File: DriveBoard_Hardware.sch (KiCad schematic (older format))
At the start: 8 parts

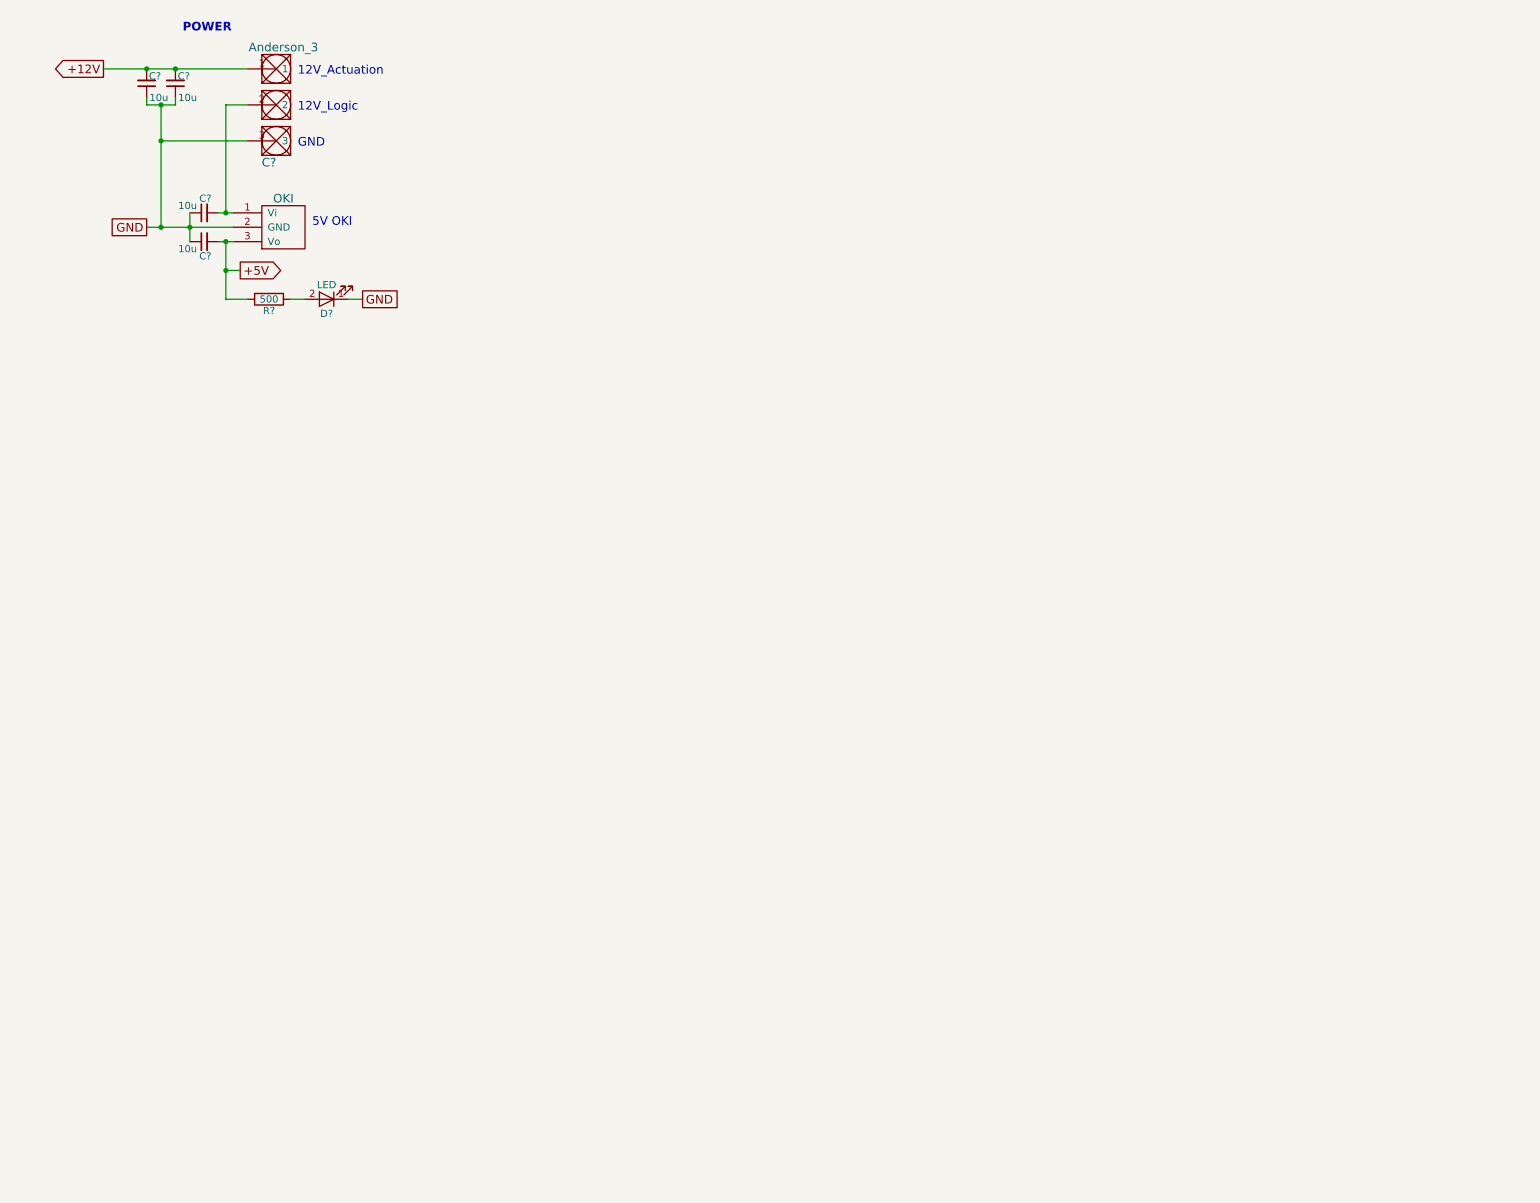
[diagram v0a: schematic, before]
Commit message: Drive Serial Added
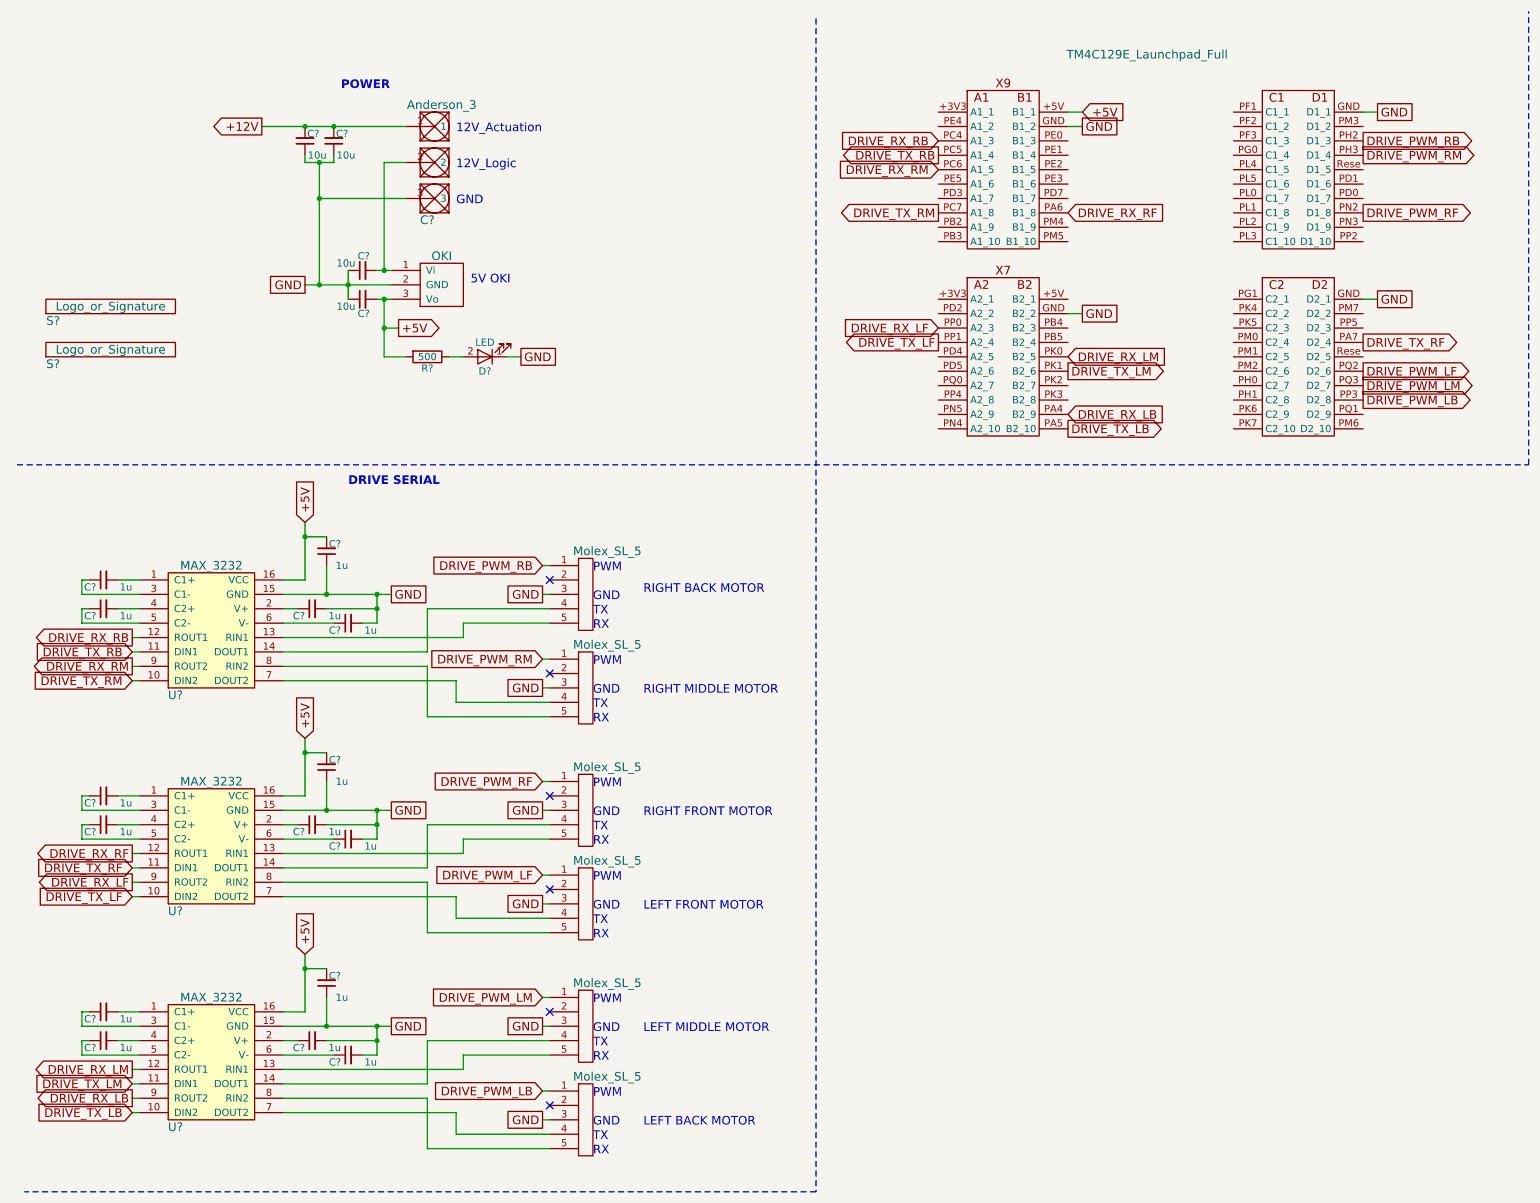
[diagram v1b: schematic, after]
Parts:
- added C? (x15): 1u, symbol C_Small
- added S? (x2): Logo_or_Signature, symbol Logo_or_Signature
- added U? (x3): MAX_3232, symbol MAX_3232
- added U? (x6): Molex_SL_5, symbol Molex_SL_5
- added U?: TM4C129E_Launchpad_Full, symbol TM4C129E_Launchpad_Full
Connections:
- net +5V: now also C?.2, C?.2, C?.2, U?.+5V (B2_1), U?.16 (VCC), U?.16 (VCC), U?.16 (VCC)
- net GND: now also C?.1, C?.1, C?.1, C?.2, C?.2, C?.2, C?.2, C?.2, C?.2, U?.15 (GND), U?.15 (GND), U?.15 (GND), U?.3, U?.3, U?.3, U?.3, U?.3, U?.3, U?.GND (D2_1)
- new net: C?.2, U?.1 (C1+) (x3)
- new net: U?.13 (RIN1), U?.5 (x3)
- new net: U?.14 (DOUT1), U?.4 (x3)
- new net: C?.1, U?.2 (V+) (x3)
- new net: C?.1, U?.3 (C1-) (x3)
- new net: C?.2, U?.4 (C2+) (x3)
- new net: C?.1, U?.5 (C2-) (x3)
- new net: C?.1, U?.6 (V-) (x3)
- new net: U?.4, U?.7 (DOUT2) (x3)
- new net: U?.5, U?.8 (RIN2) (x3)
- new net DRIVE_PWM_LB: U?.1, U?.PP3 (D2_8)
- new net DRIVE_PWM_LF: U?.1, U?.PQ2 (D2_6)
- new net DRIVE_PWM_LM: U?.1, U?.PQ3 (D2_7)
- new net DRIVE_PWM_RB: U?.1, U?.PH2 (D1_3)
- new net DRIVE_PWM_RF: U?.1, U?.PN2 (D1_8)
- new net DRIVE_PWM_RM: U?.1, U?.PH3 (D1_4)
- new net DRIVE_RX_LB: U?.9 (ROUT2), U?.PA4 (B2_9)
- new net DRIVE_RX_LF: U?.9 (ROUT2), U?.PP0 (A2_3)
- new net DRIVE_RX_LM: U?.12 (ROUT1), U?.PK0 (B2_5)
- new net DRIVE_RX_RB: U?.12 (ROUT1), U?.PC4 (A1_3)
- new net DRIVE_RX_RF: U?.12 (ROUT1), U?.PA6 (B1_8)
- new net DRIVE_RX_RM: U?.9 (ROUT2), U?.PC6 (A1_5)
- new net DRIVE_TX_LB: U?.10 (DIN2), U?.PA5 (B2_10)
- new net DRIVE_TX_LF: U?.10 (DIN2), U?.PP1 (A2_4)
- new net DRIVE_TX_LM: U?.11 (DIN1), U?.PK1 (B2_6)
- new net DRIVE_TX_RB: U?.11 (DIN1), U?.PC5 (A1_4)
- new net DRIVE_TX_RF: U?.11 (DIN1), U?.PA7 (D2_4)
- new net DRIVE_TX_RM: U?.10 (DIN2), U?.PC7 (A1_8)
- no-connect marks 0 -> 6
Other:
- note added: "DRIVE SERIAL"
- note added: "LEFT BACK MOTOR"
- note added: "LEFT FRONT MOTOR"
- note added: "LEFT MIDDLE MOTOR"
- note added: "PWM"
- note added: "RIGHT BACK MOTOR"
- note added: "RIGHT FRONT MOTOR"
- note added: "RIGHT MIDDLE MOTOR"
- note added: "RX"
- note added: "TX"
- moved on the sheet: C?, D?, R?

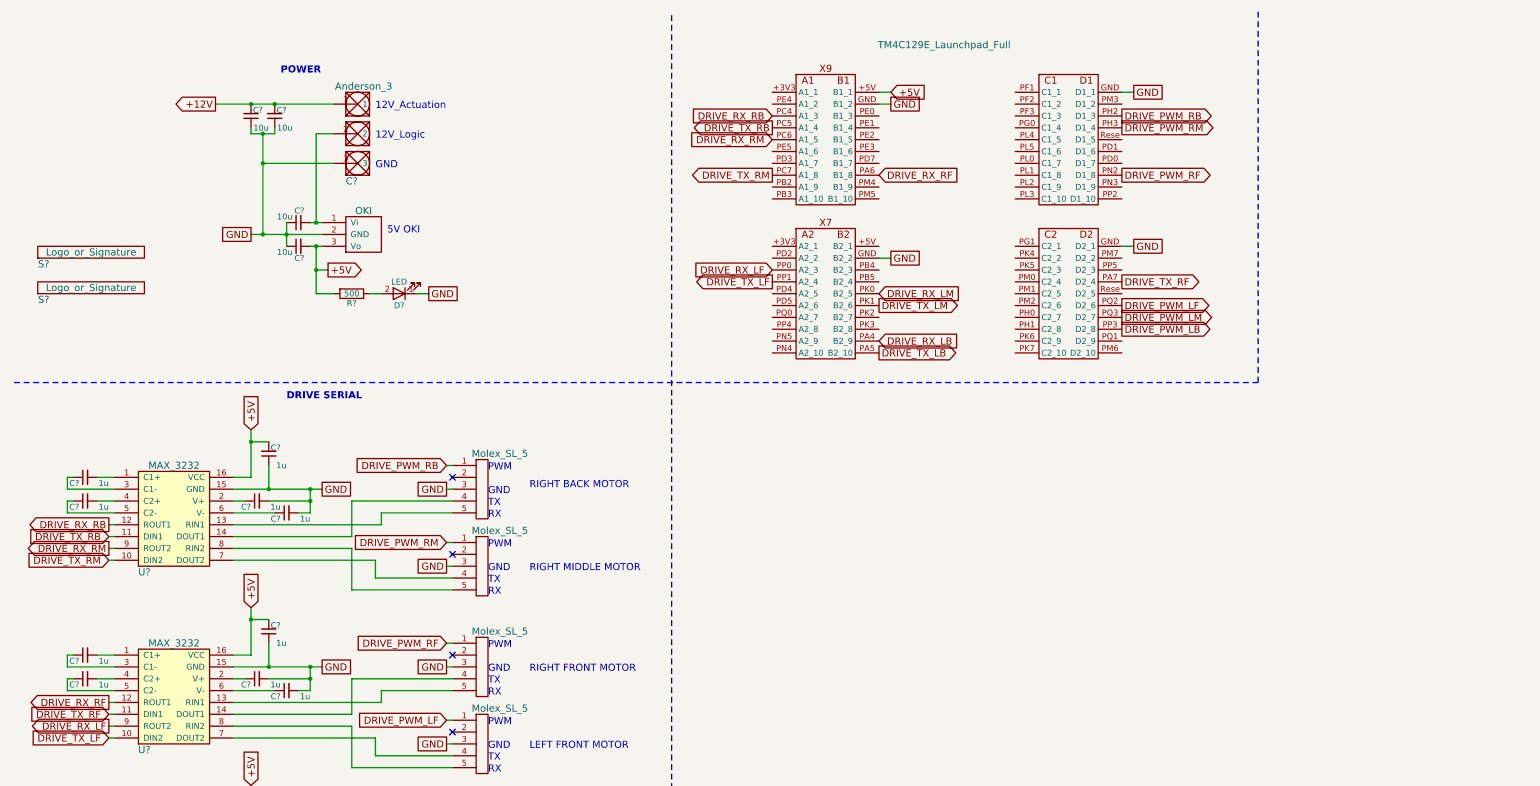
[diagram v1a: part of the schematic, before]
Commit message: Added LED Light Strips
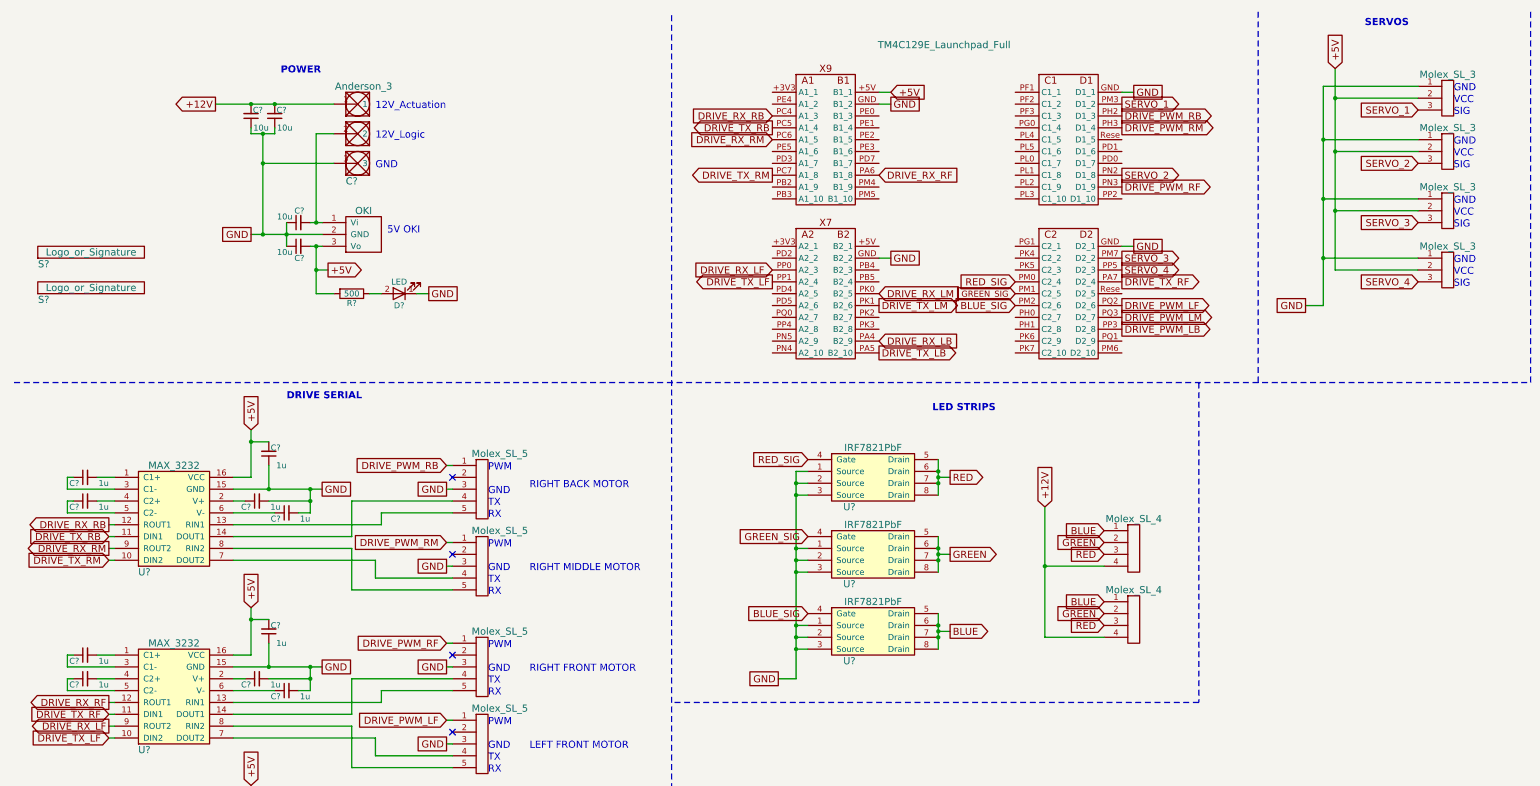
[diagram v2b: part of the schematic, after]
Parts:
- added U? (x4): Molex_SL_3, symbol Molex_SL_3
- added U? (x3): IRF7821PbF, symbol IRF7821PbF
- added U? (x2): Molex_SL_4, symbol Molex_SL_4
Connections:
- net +12V: now also U?.4, U?.4
- net +5V: now also U?.2, U?.2, U?.2, U?.2
- net DRIVE_PWM_RF: now also U?.PN3 (D1_9); no longer U?.PN2 (D1_8)
- net GND: now also U?.1, U?.1, U?.1, U?.1, U?.1 (Source), U?.1 (Source), U?.1 (Source), U?.2 (Source), U?.2 (Source), U?.2 (Source), U?.3 (Source), U?.3 (Source), U?.3 (Source)
- net RED_SIG: now reaches U?.PM0 (C2_4)
- net RED_SIG: now also U?.4 (Gate)
- net GREEN_SIG: now reaches U?.PM1 (C2_5)
- net GREEN_SIG: now also U?.4 (Gate)
- net BLUE_SIG: now reaches U?.PM2 (C2_6)
- net BLUE_SIG: now also U?.4 (Gate)
- net SERVO_1: now reaches U?.PM3 (D1_2)
- net SERVO_1: now also U?.3
- net SERVO_3: now reaches U?.PM7 (D2_2)
- net SERVO_3: now also U?.3
- net SERVO_4: now reaches U?.PP5 (D2_3)
- net SERVO_4: now also U?.3
- new net BLUE: U?.1, U?.1, U?.5 (Drain), U?.6 (Drain), U?.7 (Drain), U?.8 (Drain)
- new net GREEN: U?.2, U?.2, U?.5 (Drain), U?.6 (Drain), U?.7 (Drain), U?.8 (Drain)
- new net RED: U?.3, U?.3, U?.5 (Drain), U?.6 (Drain), U?.7 (Drain), U?.8 (Drain)
- new net SERVO_2: U?.3, U?.PN2 (D1_8)
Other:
- note added: "LED STRIPS"
- note added: "SERVOS"
- note added: "SIG"
- note added: "VCC\n"

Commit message: Schematic complete and txt file added
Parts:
- added C?: Anderson_2, symbol Anderson_2
- added SW?: SW_DPDT_x2, symbol SW_DPDT_x2
- added U? (x2): LDD-1500L_LED_DRIVER, symbol LDD-1500L_LED_DRIVER
- added U?: Headlight_1, symbol Molex_SL_2
- added U?: Headlight_2, symbol Molex_SL_2
- U?: value Molex_SL_5 -> Right Back
- U?: value Molex_SL_5 -> Right Middle
- U?: value Molex_SL_5 -> Right Front
- U?: value Molex_SL_5 -> Left Front
- U?: value Molex_SL_5 -> Left Middle
- U?: value Molex_SL_5 -> Left Back
- U?: value Molex_SL_3 -> Servo_1
- U?: value Molex_SL_3 -> Servo_2
- U?: value Molex_SL_3 -> Servo_3
- U?: value Molex_SL_3 -> Servo_4
- U?: value Molex_SL_4 -> Strip_1
- U?: value Molex_SL_4 -> Strip_2
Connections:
- net +12V: now also C?.3, SW?.1 (A); no longer C?.1
- net GND: now also C?.1, C?.2, U?.1 (-Vin), U?.1 (-Vin), U?.2 (-Vin), U?.2 (-Vin); no longer C?.3
- net HEADLIGHT_CNTR: now reaches U?.PM6 (D2_10)
- net HEADLIGHT_CNTR: now also U?.21 (ON/OFF_&_DIMMING), U?.21 (ON/OFF_&_DIMMING)
- new net: U?.11 (-Vout), U?.12 (-Vout), U?.2 (x2)
- new net: U?.1, U?.13 (+Vout), U?.14 (+Vout) (x2)
- new net HEADLIGHT_PWR: SW?.2 (B), U?.23 (+Vin), U?.23 (+Vin), U?.24 (+Vin), U?.24 (+Vin)
- new net PVDD: SW?.3 (C)
- new net PVVD: C?.1
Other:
- note added: "LED HEADLIGHT POWER SOURCE SELECT"
- note added: "LED HEADLIGHTS"
- moved on the sheet: C?

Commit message: Finished Board Layout
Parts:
- removed S? (x2): Logo_or_Signature, symbol Logo_or_Signature
- C1, C10, C11, C12, C13, C14, C15, C16, C17, C18, C19, C2, C3, C4, C5, C6, C7, C8, C9: renamed from C?; footprint (none) -> Capacitors_SMD:C_0603_HandSoldering
- C20: renamed from C?; footprint (none) -> MRDT_Connectors:Anderson_3_Horisontal_Side_by_Side
- C21: renamed from C?; footprint (none) -> MRDT_Connectors:Anderson_2_Horisontal_Side_by_Side
- D1: renamed from D?; footprint (none) -> LEDs:LED_1206_HandSoldering
- R1: renamed from R?; footprint (none) -> Resistors_SMD:R_0603_HandSoldering
- SW1: renamed from SW?; footprint (none) -> MRDT_Switches:1P2T_Angled_Slide_GPI-152-3013
- U1, U2, U3: renamed from U?; footprint (none) -> MRDT_ICs:SOIC_16_3.9x9.9mm_Pitch1.27mm
- U10, U5, U6, U7, U8, U9: renamed from U?; footprint (none) -> MRDT_Connectors:MOLEX_SL_5_Horizontal
- U11: renamed from U?; footprint (none) -> MRDT_Shields:TM4C129E_Launchpad_FULL_Booster_Bottom_SMD
- U12, U13, U14: renamed from U?; footprint (none) -> Housings_SOIC:SO-8_5.3x6.2mm_Pitch1.27mm
- U15, U16: renamed from U?; footprint (none) -> MRDT_Connectors:MOLEX_SL_4_Horizontal
- U17, U18, U19, U20: renamed from U?; footprint (none) -> MRDT_Connectors:MOLEX_SL_3_Vertical
- U21, U22: renamed from U?; footprint (none) -> MRDT_Devices:LDD-1500L_LED_DRIVER
- U23, U24: renamed from U?; footprint (none) -> MRDT_Connectors:MOLEX_SL_2_Vertical
- U4: renamed from U?; footprint (none) -> MRDT_Devices:OKI_Horisontal
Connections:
- net PVVD is gone; now on net PVDD: C21.1
- net 12V_Log: now reaches C18.2, C20.2, U4.1 (Vi)

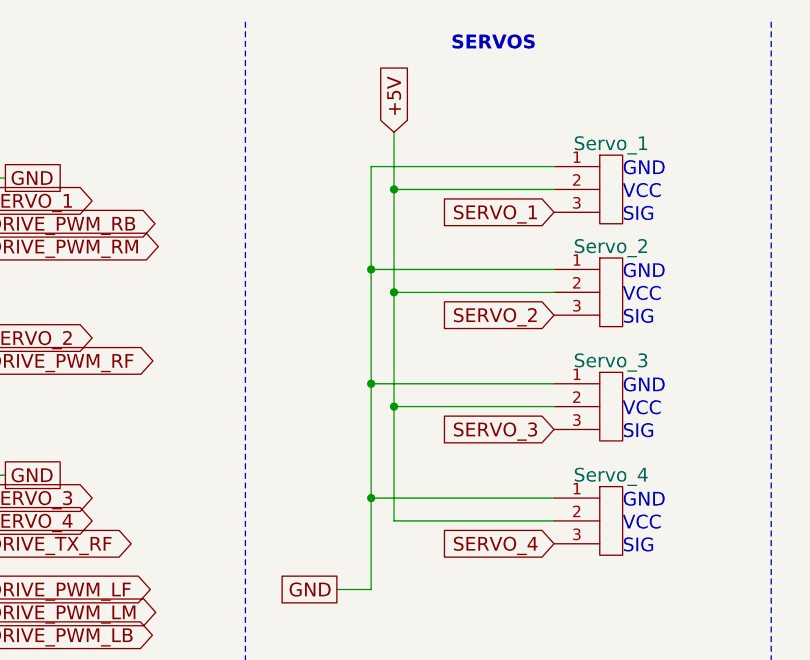
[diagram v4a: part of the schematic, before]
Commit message: Edited Schematic and added silkscreen
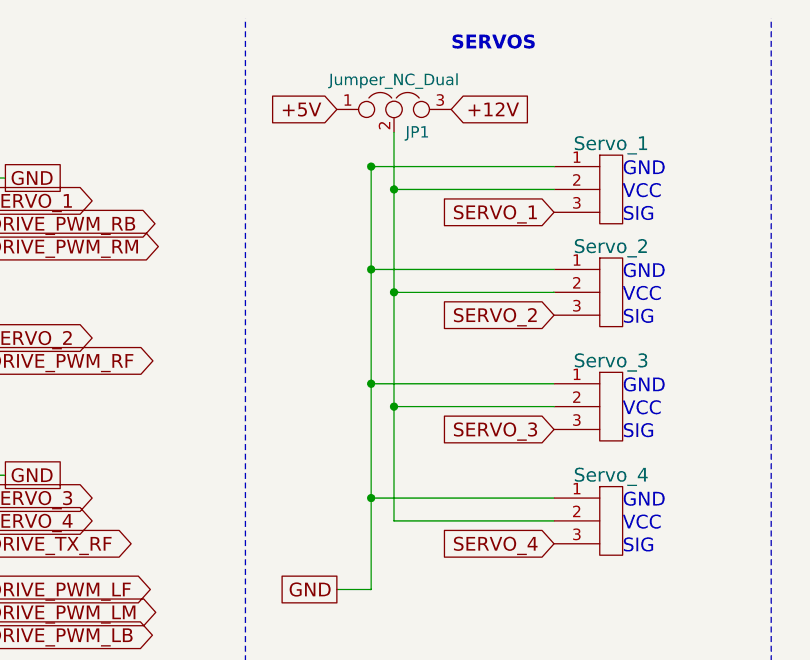
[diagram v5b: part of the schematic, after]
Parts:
- added JP1: Jumper_NC_Dual, Pin_Headers:Pin_Header_Angled_1x03_Pitch1.27mm, symbol Jumper_NC_Dual
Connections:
- net +12V: now also JP1.3
- net +5V: now also JP1.1; no longer U17.2, U18.2, U19.2, U20.2
- new net: JP1.2, U17.2, U18.2, U19.2, U20.2
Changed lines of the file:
@@
 Text GLabel 11400 3000 0    60   UnSpc ~ 0
 GND
-Text GLabel 11650 1000 1    60   Input ~ 0
+Text GLabel 11400 900  0    60   Input ~ 0
 +5V
 Wire Wire Line
@@
 Connection ~ 11650 1700
 Wire Wire Line
-	12350 1150 11550 1150
-Wire Wire Line
-	11550 1150 11550 3000
+	11550 1150 12350 1150
 Wire Wire Line
 	11550 3000 11400 3000
 Wire Wire Line
-	12350 2600 11550 2600
+	11550 2600 12350 2600
 Connection ~ 11550 2600
 Wire Wire Line
-	12350 2100 11550 2100
+	11550 2100 12350 2100
 Connection ~ 11550 2100
 Text GLabel 12350 1350 0    60   Input ~ 0
@@
 Text GLabel 3050 1550 0    60   Input ~ 0
 12V_Log
+$Comp
+L Jumper_NC_Dual JP1
+U 1 1 5AD452BD
+P 11650 900
+F 0 "JP1" H 11700 800 50  0000 L CNN
+F 1 "Jumper_NC_Dual" H 11650 1000 50  0000 C BNN
+F 2 "Pin_Headers:Pin_Header_Angled_1x03_Pitch1.27mm" H 11650 900 50  0001 C CNN
+F 3 "" H 11650 900 50  0001 C CNN
+	1    11650 900
+	1    0    0    -1
+$EndComp
+Connection ~ 11550 1150
+Wire Wire Line
+	11550 1150 11550 3000
+Text GLabel 11900 900  2    60   Input ~ 0
++12V
 $EndSCHEMATC
